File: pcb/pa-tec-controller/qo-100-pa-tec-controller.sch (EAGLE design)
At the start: 91 parts, among them CON1 2EDG-2P-5MM, CON2 2EDG-2P-5MM, CON3 2EDG-2P-5MM, CON4 2EDG-2P-5MM, CON5 2EDG-2P-5MM, U1 LT8640S, U2 LT8640S, U3 LT8640S, U4 LT8640S, U5 MCP4728-A2

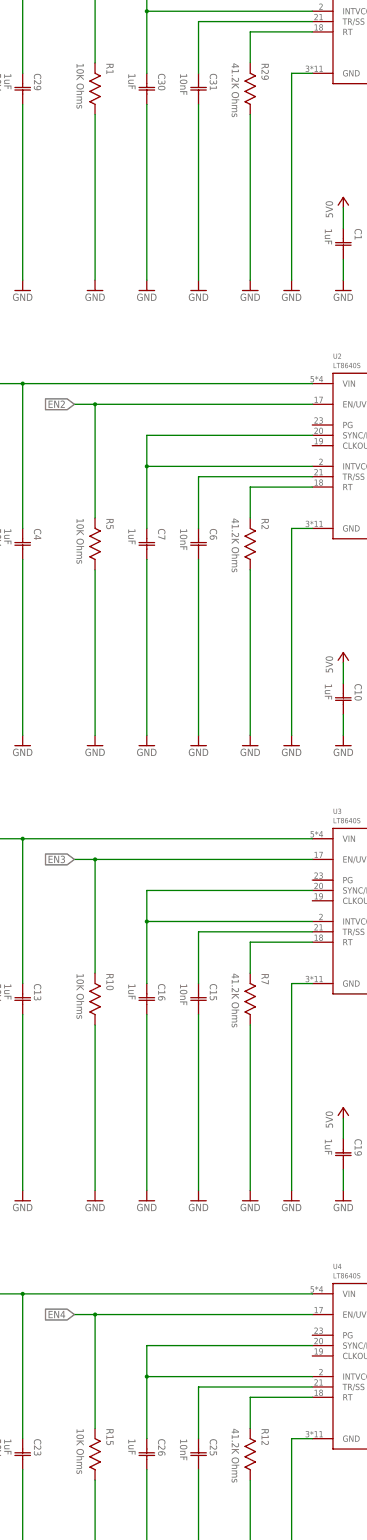
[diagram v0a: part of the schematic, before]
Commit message: PA TEC Controller assembly BOM changes
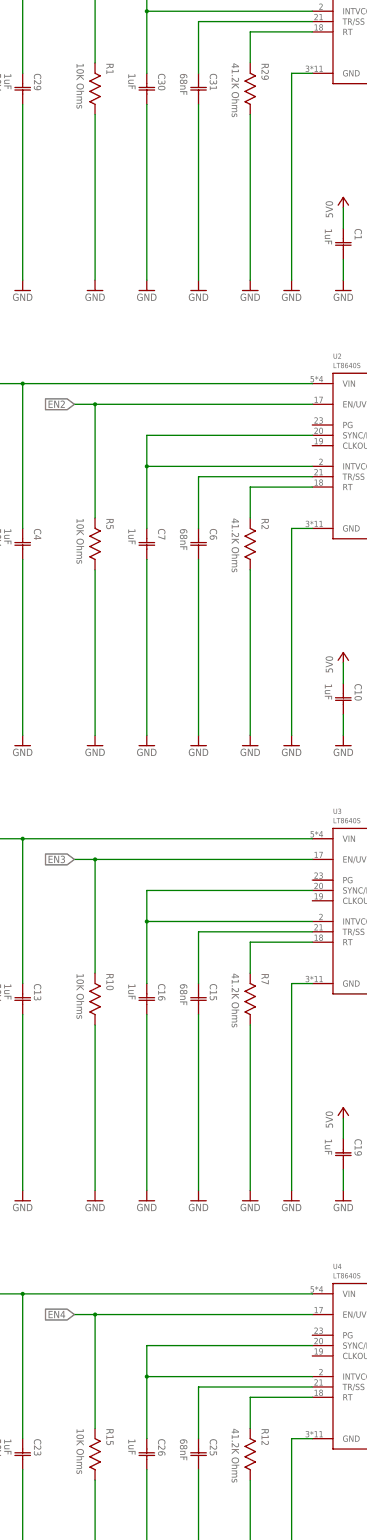
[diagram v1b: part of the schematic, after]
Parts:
- C15, C25, C31, C6: value 10nF -> 68nF
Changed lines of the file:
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@@
 <part name="GND11" library="Supply Symbol" deviceset="GND" device=""/>
 <part name="GND12" library="Supply Symbol" deviceset="GND" device=""/>
-<part name="C6" library="Capacitor" deviceset="CAPACITOR" device="-0603" value="10nF"/>
+<part name="C6" library="Capacitor" deviceset="CAPACITOR" device="-0603" value="68nF"/>
 <part name="C7" library="Capacitor" deviceset="CAPACITOR" device="-0603" value="1uF"/>
 <part name="R2" library="Resistor" deviceset="RESISTOR" device="-0603" value="41.2K Ohms"/>
@@
 <part name="GND25" library="Supply Symbol" deviceset="GND" device=""/>
 <part name="GND26" library="Supply Symbol" deviceset="GND" device=""/>
-<part name="C15" library="Capacitor" deviceset="CAPACITOR" device="-0603" value="10nF"/>
+<part name="C15" library="Capacitor" deviceset="CAPACITOR" device="-0603" value="68nF"/>
 <part name="C16" library="Capacitor" deviceset="CAPACITOR" device="-0603" value="1uF"/>
 <part name="R7" library="Resistor" deviceset="RESISTOR" device="-0603" value="41.2K Ohms"/>
@@
 <part name="GND40" library="Supply Symbol" deviceset="GND" device=""/>
 <part name="GND41" library="Supply Symbol" deviceset="GND" device=""/>
-<part name="C25" library="Capacitor" deviceset="CAPACITOR" device="-0603" value="10nF"/>
+<part name="C25" library="Capacitor" deviceset="CAPACITOR" device="-0603" value="68nF"/>
 <part name="C26" library="Capacitor" deviceset="CAPACITOR" device="-0603" value="1uF"/>
 <part name="R12" library="Resistor" deviceset="RESISTOR" device="-0603" value="41.2K Ohms"/>
@@
 <part name="GND131" library="Supply Symbol" deviceset="GND" device=""/>
 <part name="GND133" library="Supply Symbol" deviceset="GND" device=""/>
-<part name="C31" library="Capacitor" deviceset="CAPACITOR" device="-0603" value="10nF"/>
+<part name="C31" library="Capacitor" deviceset="CAPACITOR" device="-0603" value="68nF"/>
 <part name="C30" library="Capacitor" deviceset="CAPACITOR" device="-0603" value="1uF"/>
 <part name="R29" library="Resistor" deviceset="RESISTOR" device="-0603" value="41.2K Ohms"/>
